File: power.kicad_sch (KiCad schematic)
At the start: 89 parts, among them Q1 PJE138K, Q2 PJE138K, Q3 SSM3J332R, Q4 PJE138K, Q5 SSM3J332R, Q6 PJE138K, Q7 SSM3J332R, U1 TLV70018_SC70, U4 TPS65150_HTSSOP, U5 MPQ7235GQBE, U6 TLV76701_WSON

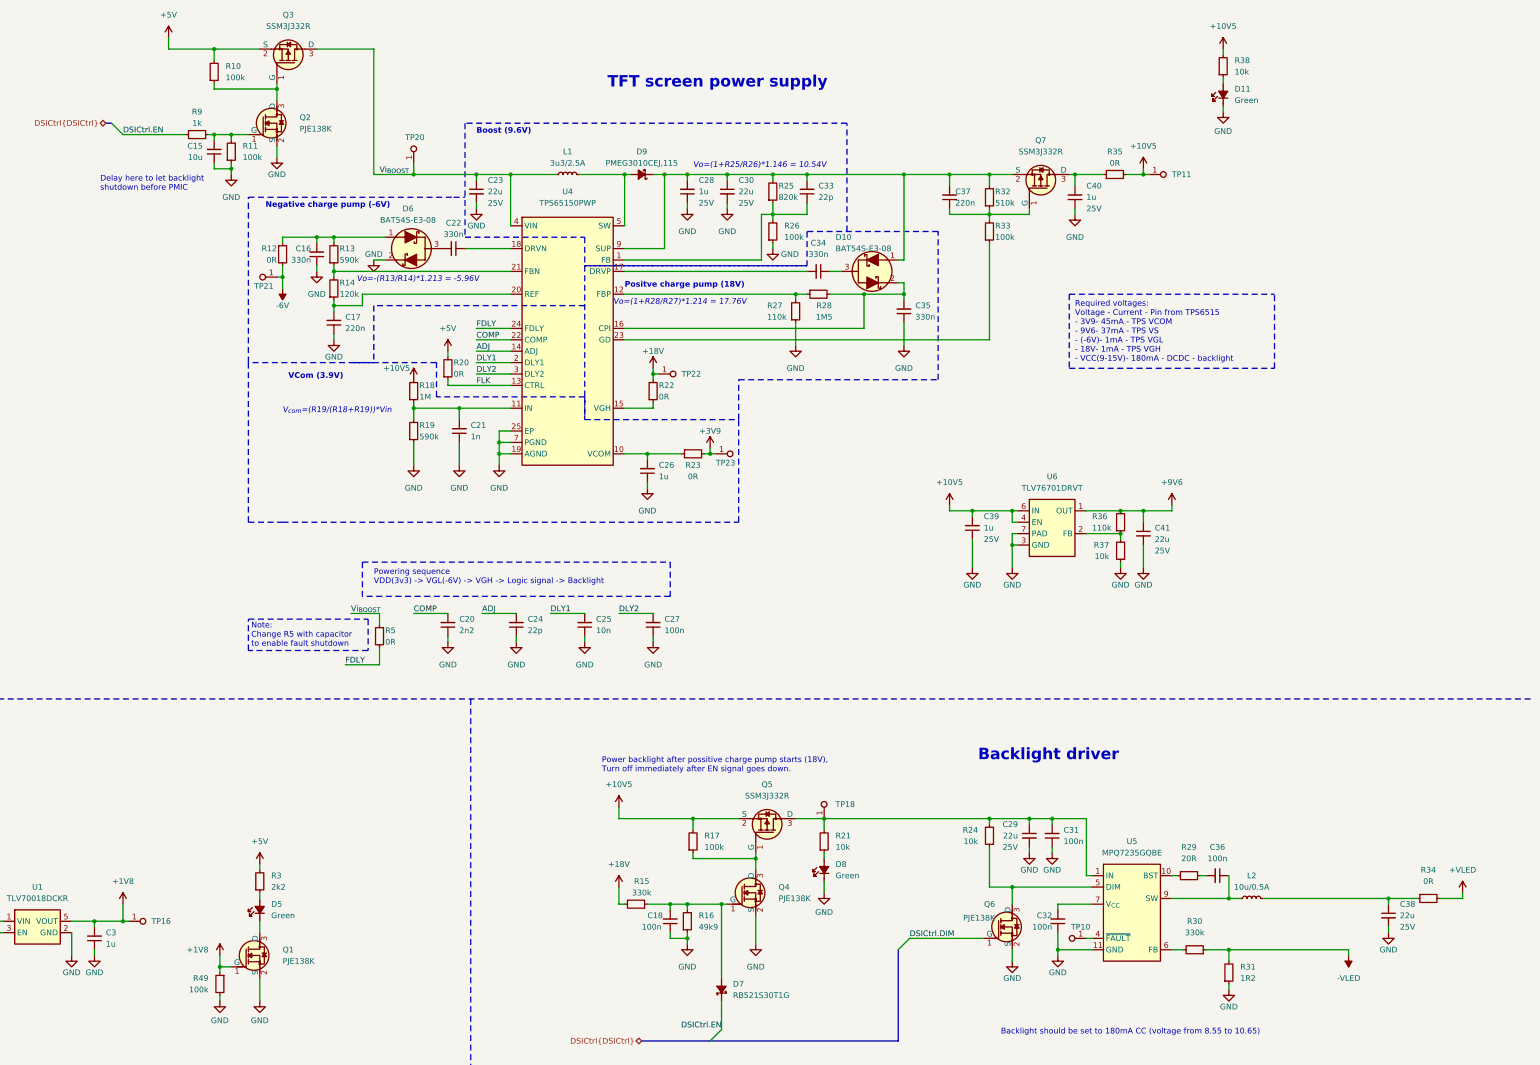
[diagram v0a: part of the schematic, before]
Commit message: [#73840] Bump rev to 1.1.3, Standarize Sch
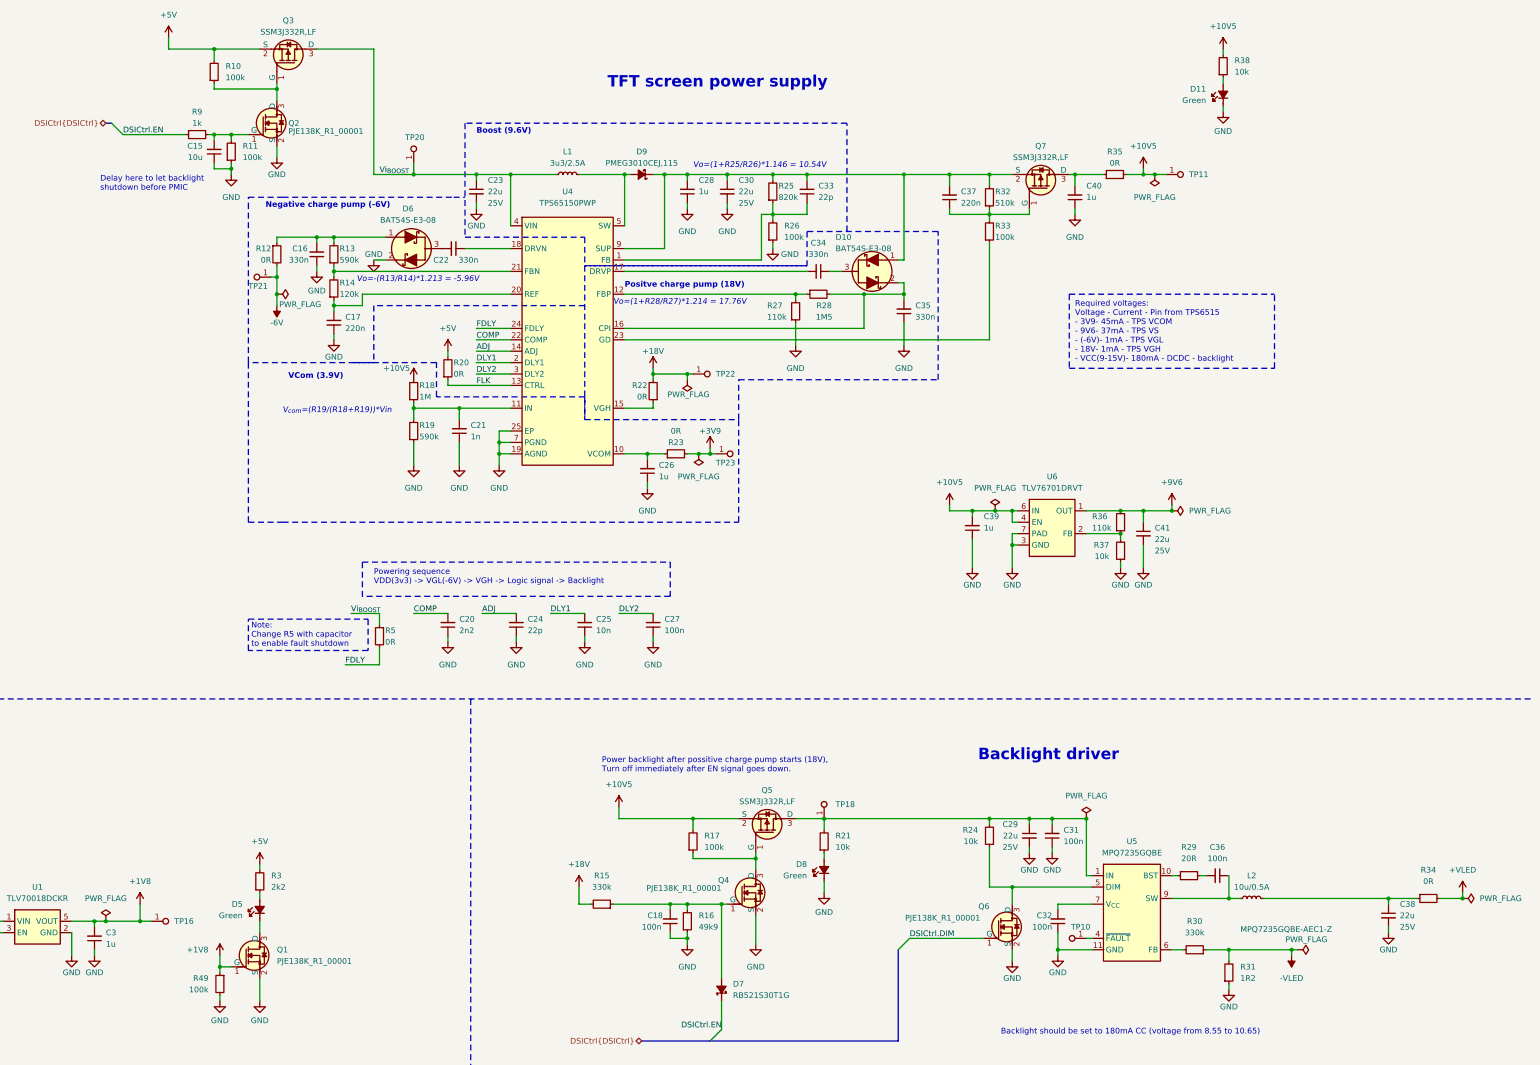
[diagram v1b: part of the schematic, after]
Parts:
- C15, C16, C17, C18, C2, C20, C21, C22, C24, C25, C26, C27, C28, C3, C31, C32, C33, C34, C35, C36, C37, C39, C40, D7, D9, L1, L2, R10, R11, R12, R13, R14, R15, R16, R17, R18, R19, R20, R21, R22, R23, R24, R25, R26, R27, R28, R29, R3, R30, R31, R32, R33, R34, R35, R36, R37, R38, R49, R9, TP11, TP16, TP20: Public False -> (none)
- D11, D5, D8: footprint antmicro-footprints:LED_0603_1608Metric_G -> antmicro-footprints:LED_0603_1608Metric_G_Right_Angle; Public False -> (none)
- TP10, TP18, TP21, TP22, TP23: Public False -> (none); now left out of the parts list
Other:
- moved on the sheet: C16, R12, R15, R22, R23, TP11, TP16, TP21, TP22

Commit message: [#73840] Change right angle LEDs to vertical (KP-1608ZGC)
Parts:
- removed D11, D5, D8: LED_G_0603_598-8D80-107F, antmicro-footprints:LED_0603_1608Metric_G_Right_Angle, symbol antmicroLEDIndicationDiscrete:LED_G_0603_598-8D80-107F
- removed R21, R38: R_10k_0402, antmicro-footprints:R_0402_1005Metric, symbol antmicroResistors0402:R_10k_0402
- removed R3: R_2k2_0402, antmicro-footprints:R_0402_1005Metric, symbol antmicroResistors0402:R_2k2_0402
- added D11, D5, D8: LED_G_0603_KP-1608ZGC, antmicro-footprints:LED_0603_1608Metric_G, symbol antmicroLEDIndicationDiscrete:LED_G_0603_KP-1608ZGC
- added R2, R21: R_1k_0402, antmicro-footprints:R_0402_1005Metric, symbol antmicroResistors0402:R_1k_0402
- added R38: R_470R_0402, antmicro-footprints:R_0402_1005Metric, symbol antmicroResistors0402:R_470R_0402
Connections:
- net +10V5: now also D5.2 (A)
- net +5V: now also D8.2 (A)
- net GND: now also R2.1, R21.1
- net at C29.1, C31.2, Q5.3 (D)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: now also D11.2 (A)
- net at Q1.3 (D): now also R38.1
- new net: D8.1 (C), R38.2
- new net: D5.1 (C), R2.2
- new net: D11.1 (C), R21.2

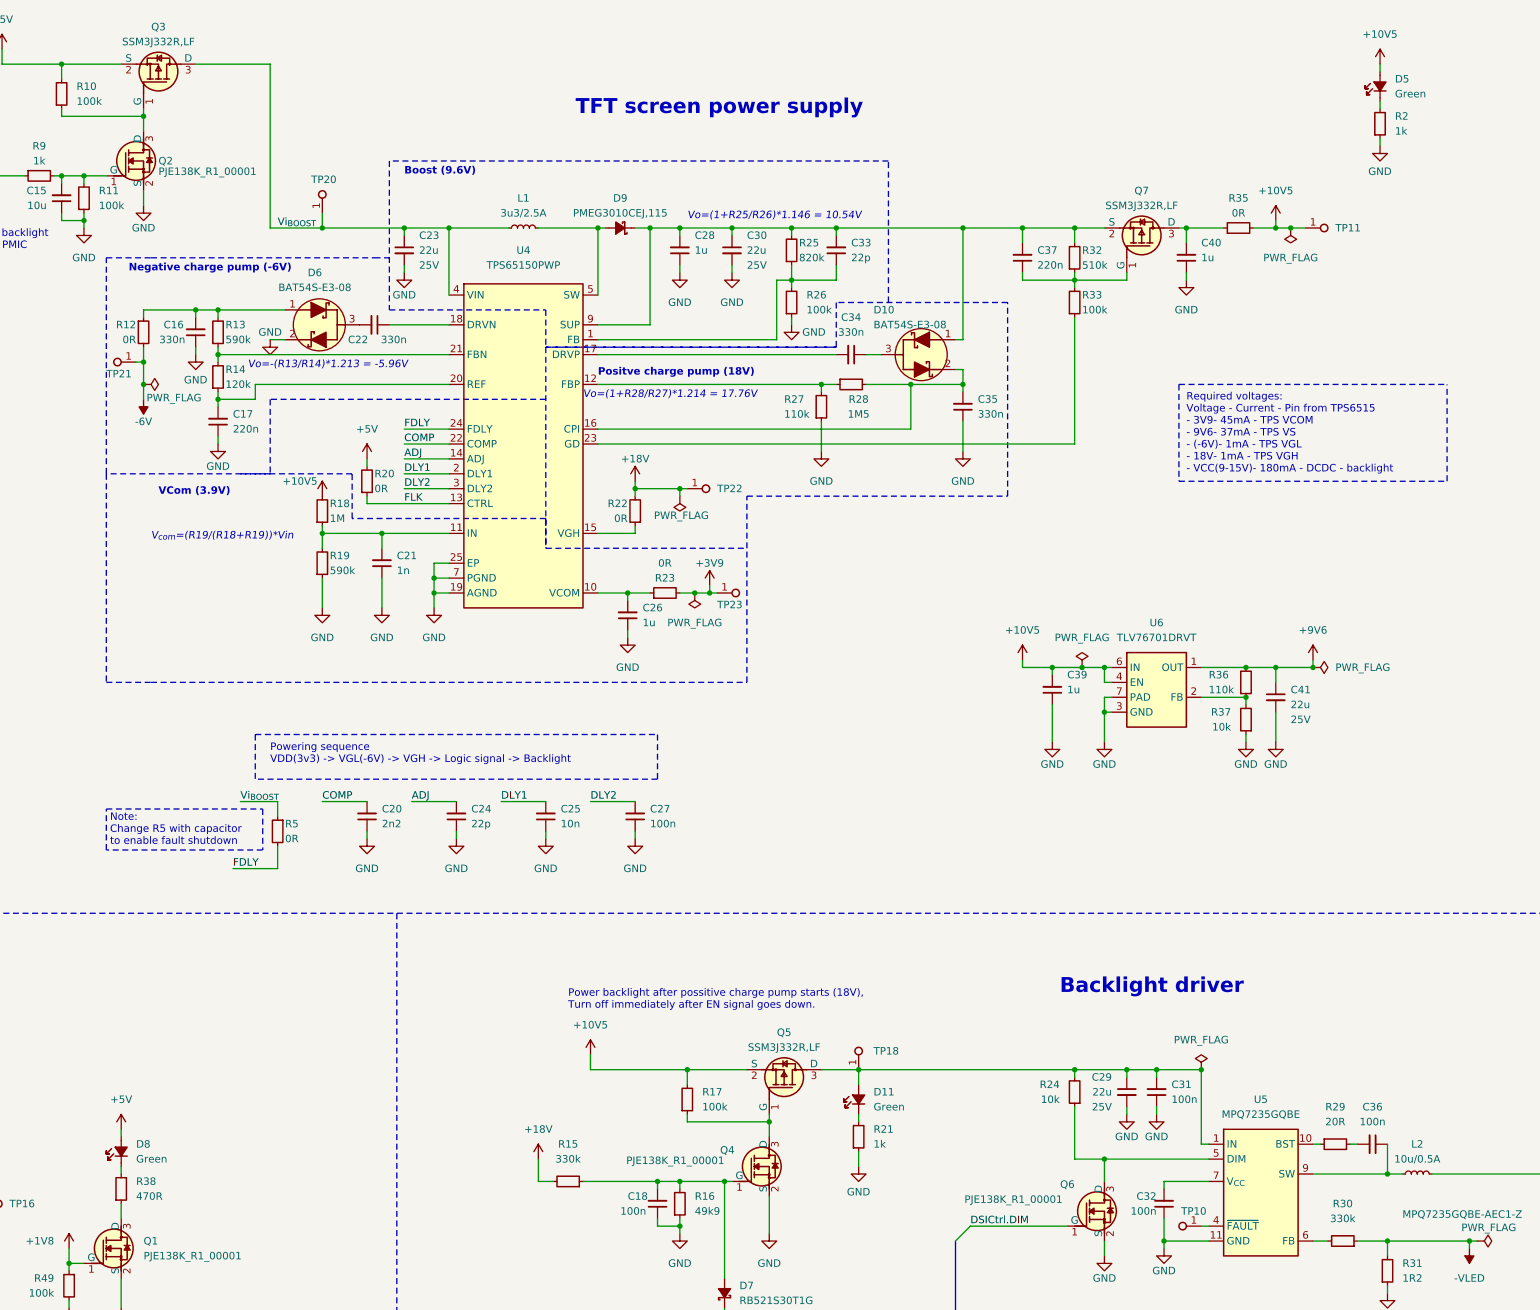
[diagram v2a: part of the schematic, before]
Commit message: [#73840] Update LEDs on PCB
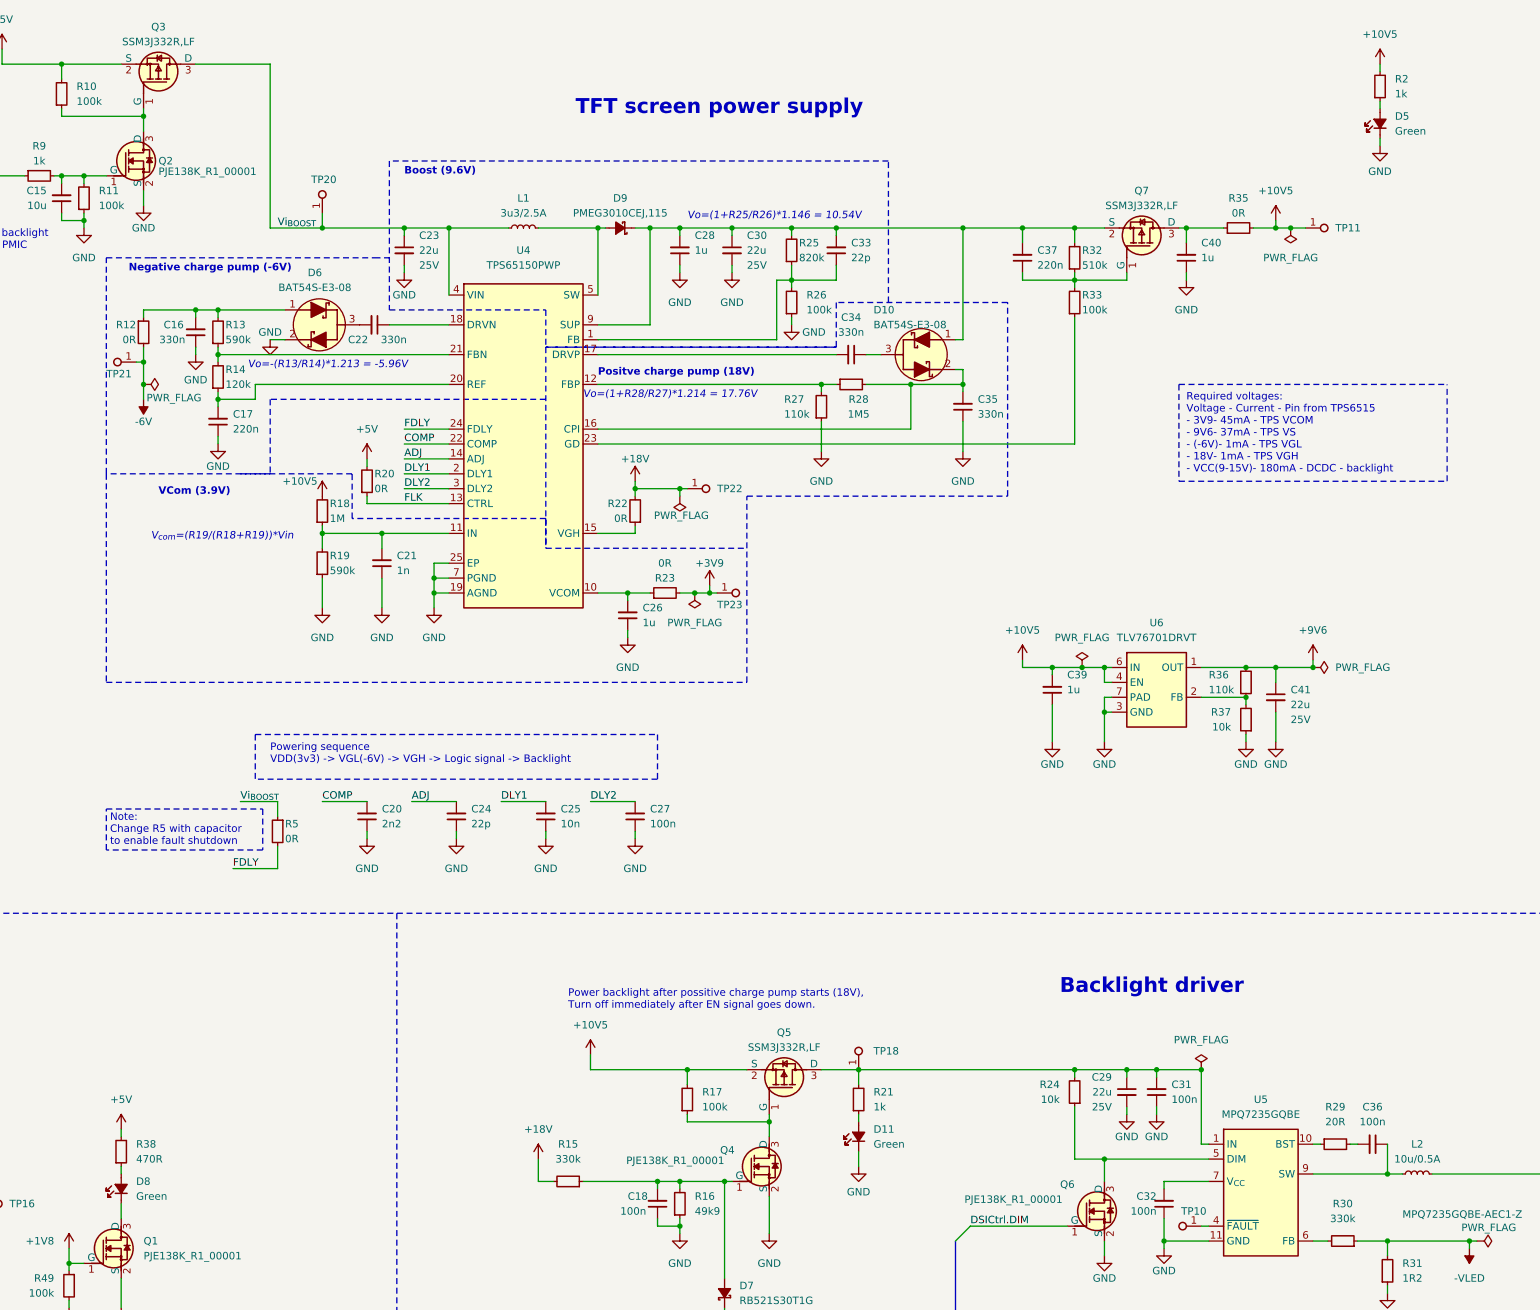
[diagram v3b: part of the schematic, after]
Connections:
- net +10V5: now also R2.2; no longer D5.2 (A)
- net +5V: now also R38.2; no longer D8.2 (A)
- net GND: now also D11.1 (C), D5.1 (C); no longer R2.1, R21.1
- net at D8.1 (C): now also Q1.3 (D); no longer R38.2
- net at C29.1, C31.2, Q5.3 (D)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: now also R21.2; no longer D11.2 (A)
- net at R38.1: now also D8.2 (A); no longer Q1.3 (D)
- new net: D5.2 (A), R2.1
- new net: D11.2 (A), R21.1
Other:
- moved on the sheet: D11, D5, D8, R2, R21, R38
